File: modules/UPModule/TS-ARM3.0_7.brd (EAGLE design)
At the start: 42.3 x 27.4 mm, 83 parts, among them IC1 LPC1115, IC100 BD9G101, P1 , P10 , P11 , P12 , P13 , P14 , P2 , P3 , P4 , P5 , P6 , P7 , P8 , P9 , T1 BC856, T2 BCP52, T3 BC847, X1 EIB

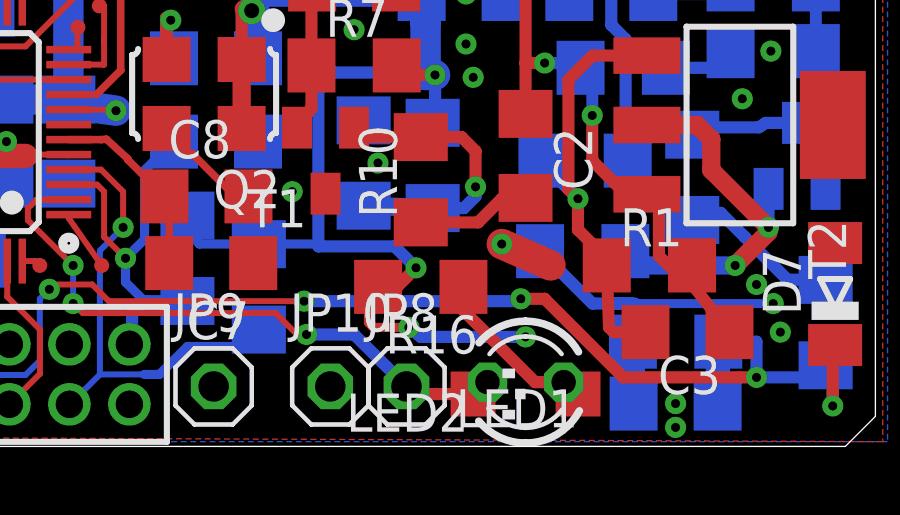
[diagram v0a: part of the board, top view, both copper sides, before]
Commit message: VCC Leiche beim progtaster entfernt
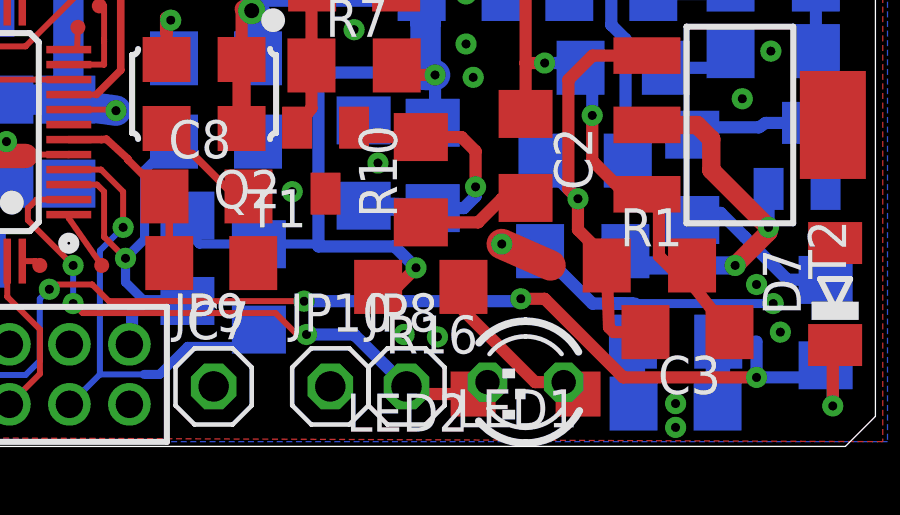
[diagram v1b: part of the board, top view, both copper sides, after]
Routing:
- net +3V3: track 118.9 -> 112.3 mm, vias 8 -> 6
- net GND: vias 43 -> 45
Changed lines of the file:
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@@
 <wire x1="18.673125" y1="13.81125" x2="18.673125" y2="12.8975" width="0.4064" layer="1"/>
 <contactref element="C14" pad="1"/>
+<via x="26.590625" y="3.730625" extent="1-16" drill="0.3"/>
+<via x="27.701875" y="3.65125" extent="1-16" drill="0.3"/>
 </signal>
 <signal name="LX">
@@
 <contactref element="C103" pad="1"/>
 <wire x1="10.9925" y1="25.0825" x2="11.31" y2="24.5675" width="1.016" layer="16"/>
-<via x="30.63875" y="3.65125" extent="1-16" drill="0.3"/>
 <wire x1="15.39875" y1="11.56" x2="13.335" y2="11.56" width="1.016" layer="16"/>
 <wire x1="16.98625" y1="11.191875" x2="15.26875" y2="11.43" width="1.016" layer="16"/>
@@
 <wire x1="7.858125" y1="21.107" x2="7.858125" y2="21.2725" width="1.016" layer="16"/>
 <wire x1="7.858125" y1="21.2725" x2="7.540625" y2="21.186375" width="1.016" layer="16"/>
-<wire x1="26.67" y1="3.96875" x2="26.749375" y2="3.96875" width="0.4064" layer="16"/>
-<via x="26.749375" y="3.96875" extent="1-16" drill="0.3" diameter="0.254"/>
 <wire x1="27.175" y1="15.08125" x2="27.175" y2="14.25875" width="0.4064" layer="16"/>
 <wire x1="27.175" y1="14.25875" x2="27.305" y2="14.12875" width="0.4064" layer="16"/>
-<wire x1="30.63875" y1="3.65125" x2="27.14625" y2="3.65125" width="0.4064" layer="16"/>
-<wire x1="27.14625" y1="3.65125" x2="26.749375" y2="3.96875" width="0.4064" layer="16"/>
 <wire x1="26.431875" y1="12.3825" x2="27.6225" y2="12.3825" width="0.4064" layer="1"/>
 <wire x1="26.431875" y1="12.3825" x2="26.34575" y2="12.7" width="0.254" layer="1"/>
@@
 <wire x1="23.733125" y1="6.746875" x2="21.7555" y2="6.746875" width="0.3048" layer="16"/>
 <wire x1="21.7555" y1="6.746875" x2="21.74875" y2="6.740125" width="0.3048" layer="16"/>
-<wire x1="26.749375" y1="3.96875" x2="25.55875" y2="3.96875" width="0.3048" layer="1"/>
-<wire x1="25.55875" y1="3.96875" x2="25.4" y2="4.1275" width="0.3048" layer="1"/>
-<wire x1="25.4" y1="4.1275" x2="25.4" y2="5.311375" width="0.3048" layer="1"/>
 <wire x1="25.4" y1="5.311375" x2="25.72425" y2="5.318125" width="0.3048" layer="1"/>
 <wire x1="19.3675" y1="7.692625" x2="19.3675" y2="7.14375" width="0.3048" layer="16"/>

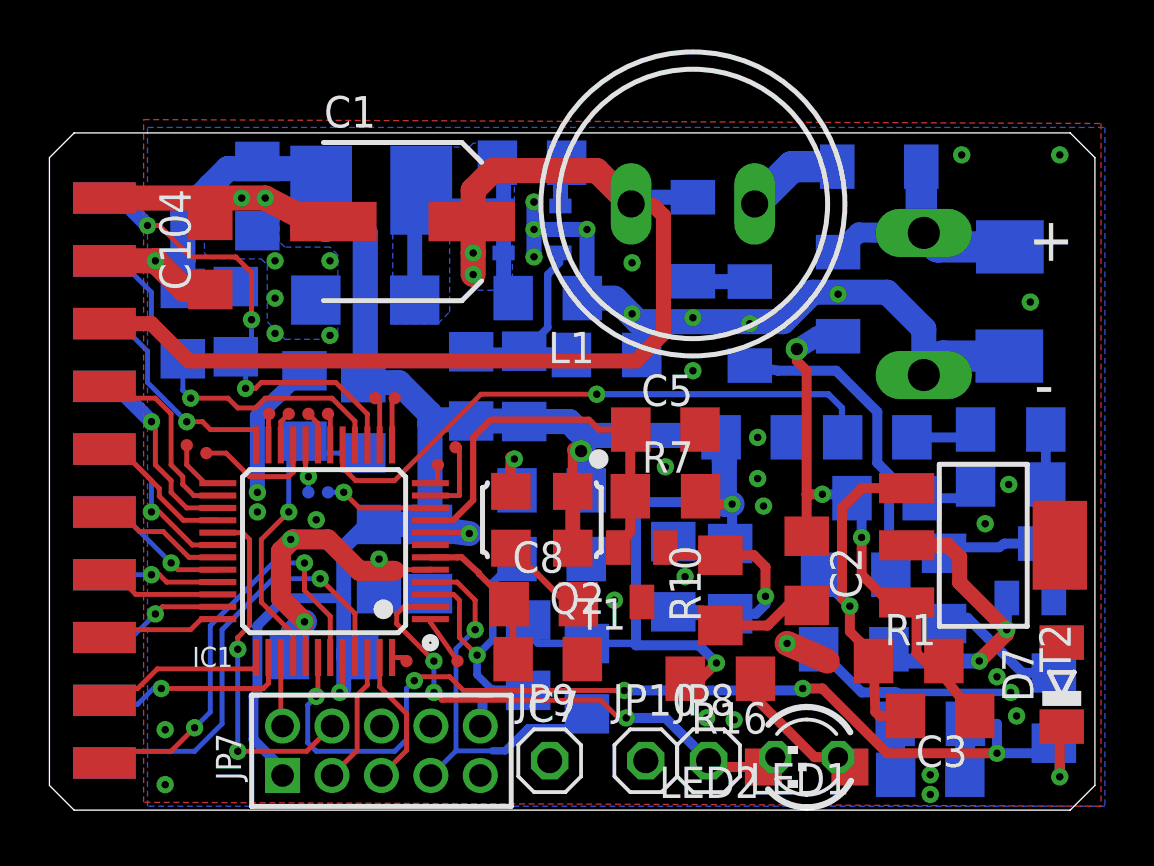
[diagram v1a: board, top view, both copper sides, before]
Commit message: Referenz vias zugefügt.
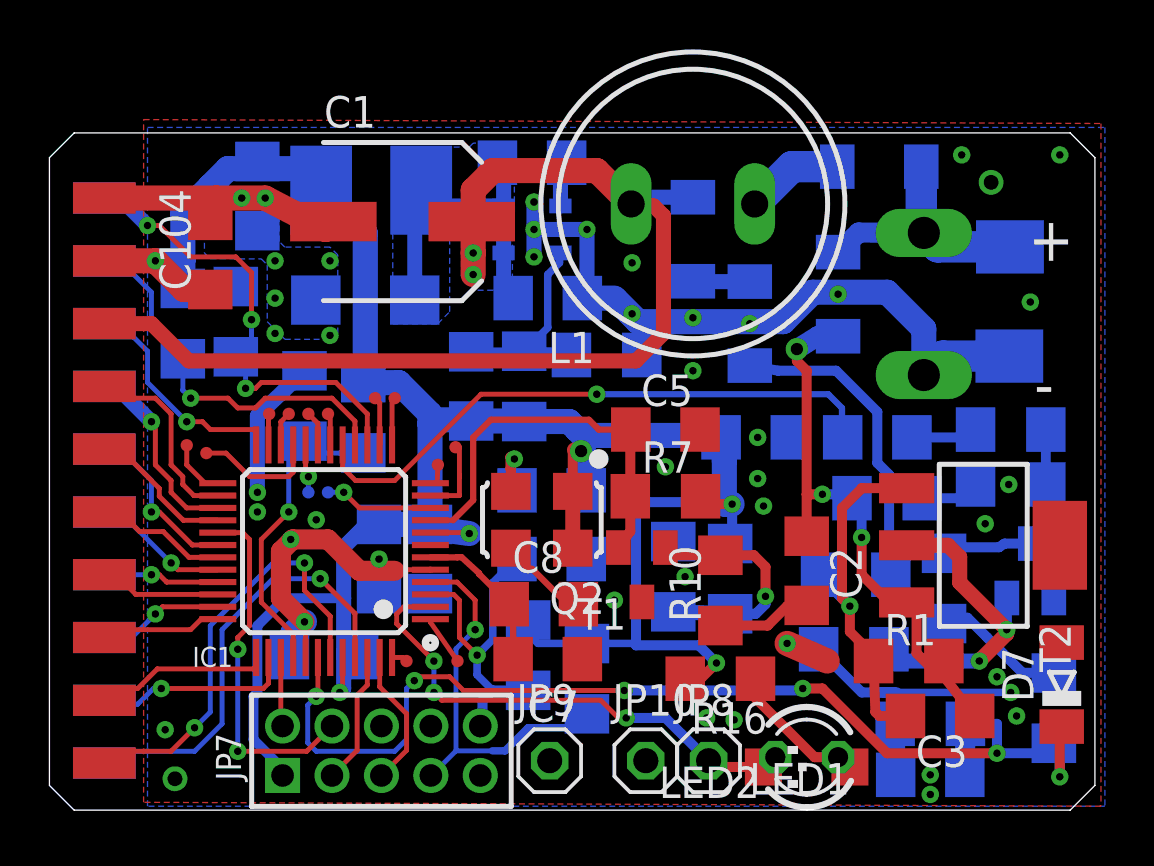
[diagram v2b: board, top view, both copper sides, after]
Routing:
- net GND: vias 45 -> 46
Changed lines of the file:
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@@
 <layer number="21" name="tPlace" color="7" fill="1" visible="yes" active="yes"/>
 <layer number="22" name="bPlace" color="7" fill="1" visible="yes" active="yes"/>
-<layer number="23" name="tOrigins" color="15" fill="1" visible="yes" active="yes"/>
-<layer number="24" name="bOrigins" color="15" fill="1" visible="yes" active="yes"/>
+<layer number="23" name="tOrigins" color="15" fill="1" visible="no" active="yes"/>
+<layer number="24" name="bOrigins" color="15" fill="1" visible="no" active="yes"/>
 <layer number="25" name="tNames" color="7" fill="1" visible="no" active="yes"/>
 <layer number="26" name="bNames" color="7" fill="1" visible="no" active="yes"/>
@@
 <contactref element="JP10" pad="1"/>
 <via x="4.683125" y="3.254375" extent="1-16" drill="0.3"/>
-<via x="4.683125" y="1.031875" extent="1-16" drill="0.3"/>
 <via x="35.639375" y="1.42875" extent="1-16" drill="0.3"/>
 <via x="35.639375" y="0.635" extent="1-16" drill="0.3"/>
@@
 <via x="26.590625" y="3.730625" extent="1-16" drill="0.3"/>
 <via x="27.701875" y="3.65125" extent="1-16" drill="0.3"/>
+<via x="5.08" y="1.27" extent="1-16" drill="0.6"/>
+<via x="38.1" y="25.4" extent="1-16" drill="0.6"/>
 </signal>
 <signal name="LX">

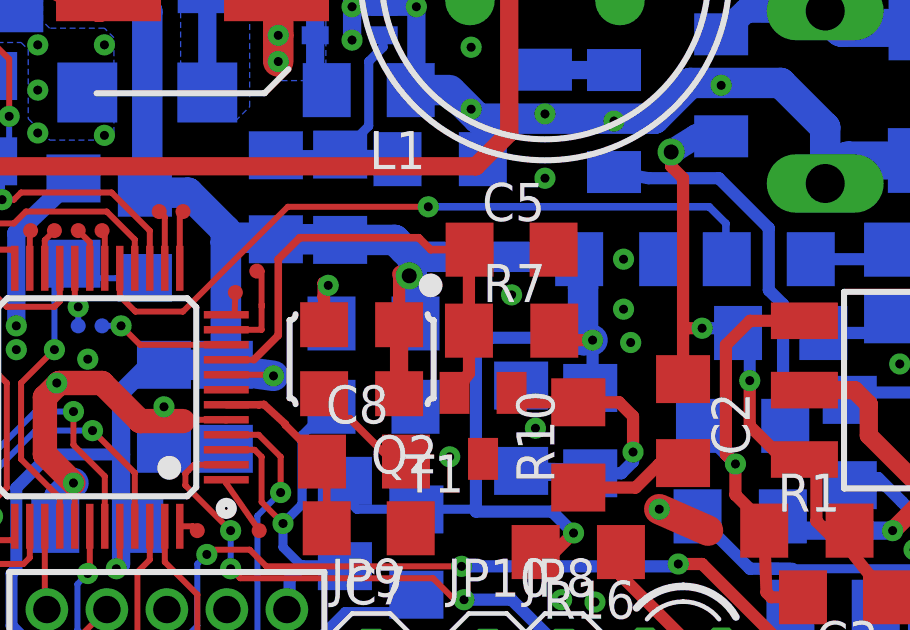
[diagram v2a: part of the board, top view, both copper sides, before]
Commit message: value cap divider changed, micro vias with tstop, and hole free on top
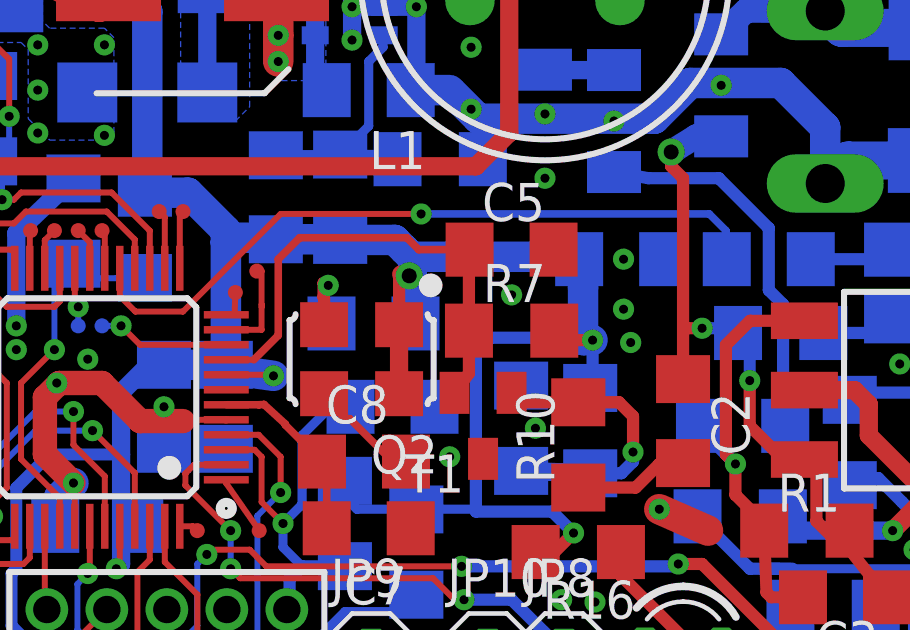
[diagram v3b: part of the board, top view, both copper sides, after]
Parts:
- C7: value 10p -> 220p
- C8: value 22p -> 100p
- moved C9 0.63 mm to (21.0, 10.2)
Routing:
- net RESET: track 13.1 -> 13.8 mm
